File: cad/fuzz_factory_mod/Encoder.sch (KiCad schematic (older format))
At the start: 15 parts

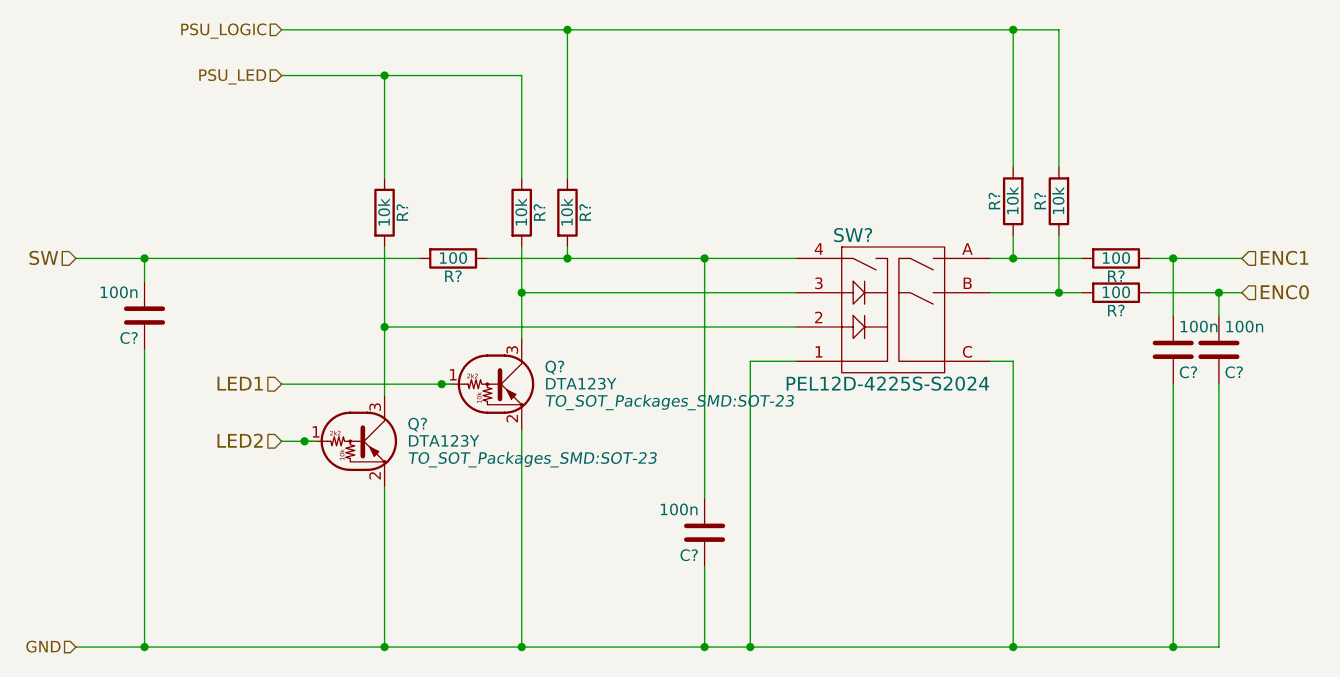
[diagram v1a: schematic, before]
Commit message: Continued schematic.
Modified fuuz_factory circuit : use of matched transistor pairs.
Added USB interface, through FT230X and direct to MCU.
Associated footprints, except for XTAL and trimmers.
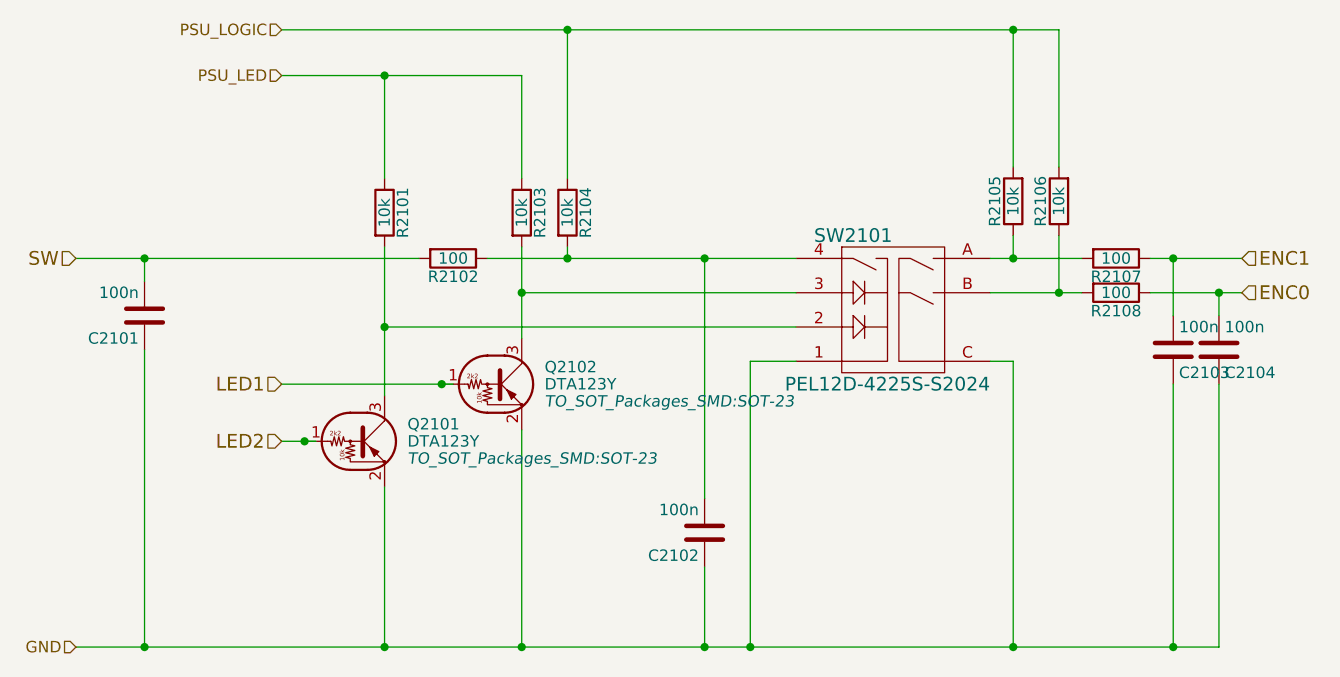
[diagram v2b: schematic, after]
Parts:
- C1901, C1902, C1903, C1904: renamed from C?; footprint Capacitors_SMD:C_0805_HandSoldering -> Capacitors_SMD:C_0603
- R1901, R1902, R1903, R1904, R1905, R1906, R1907, R1908: renamed from R?; footprint Resistors_SMD:R_0603_HandSoldering -> Resistors_SMD:R_0603
- gave numbers to parts that had none: 3

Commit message: Continued schematic.
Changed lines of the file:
@@
 $Descr A4 11693 8268
 encoding utf-8
-Sheet 20 22
+Sheet 6 26
 Title ""
 Date ""
@@
 AR Path="/5E083283/5E2DCD79/5E256B56" Ref="SW2001"  Part="1"
 AR Path="/5E083283/5E2E8544/5E256B56" Ref="SW2101"  Part="1"
-F 0 "SW2101" H 5900 4300 60  0000 C CNN
+AR Path="/5DE4AD26/5EEFDD5E/5E243285/5E256B56" Ref="SW601"  Part="1"
+AR Path="/5DE4AD26/5EEFDD5E/5E2DCD79/5E256B56" Ref="SW701"  Part="1"
+AR Path="/5DE4AD26/5EEFDD5E/5E2E8544/5E256B56" Ref="SW801"  Part="1"
+F 0 "SW801" H 5900 4300 60  0000 C CNN
 F 1 "PEL12D-4225S-S2024" H 6050 3650 60  0000 C CNN
 F 2 "flax_lib:PEL12D" H 5900 4300 60  0001 C CNN
@@
 AR Path="/5E083283/5E2DCD79/5E256B67" Ref="Q2002"  Part="1"
 AR Path="/5E083283/5E2E8544/5E256B67" Ref="Q2102"  Part="1"
-F 0 "Q2102" H 4550 3925 50  0000 L CNN
+AR Path="/5DE4AD26/5EEFDD5E/5E243285/5E256B67" Ref="Q606"  Part="1"
+AR Path="/5DE4AD26/5EEFDD5E/5E2DCD79/5E256B67" Ref="Q702"  Part="1"
+AR Path="/5DE4AD26/5EEFDD5E/5E2E8544/5E256B67" Ref="Q804"  Part="1"
+F 0 "Q804" H 4550 3925 50  0000 L CNN
 F 1 "DTA123Y" H 4550 3850 50  0000 L CNN
 F 2 "TO_SOT_Packages_SMD:SOT-23" H 4550 3775 50  0000 L CIN
@@
 AR Path="/5E083283/5E2DCD79/5E256B6D" Ref="Q2001"  Part="1"
 AR Path="/5E083283/5E2E8544/5E256B6D" Ref="Q2101"  Part="1"
-F 0 "Q2101" H 3950 4175 50  0000 L CNN
+AR Path="/5DE4AD26/5EEFDD5E/5E243285/5E256B6D" Ref="Q605"  Part="1"
+AR Path="/5DE4AD26/5EEFDD5E/5E2DCD79/5E256B6D" Ref="Q701"  Part="1"
+AR Path="/5DE4AD26/5EEFDD5E/5E2E8544/5E256B6D" Ref="Q803"  Part="1"
+F 0 "Q803" H 3950 4175 50  0000 L CNN
 F 1 "DTA123Y" H 3950 4100 50  0000 L CNN
 F 2 "TO_SOT_Packages_SMD:SOT-23" H 3950 4025 50  0000 L CIN
@@
 AR Path="/5E083283/5E2DCD79/5E256B73" Ref="R2004"  Part="1"
 AR Path="/5E083283/5E2E8544/5E256B73" Ref="R2104"  Part="1"
-F 0 "R2104" V 4730 3100 50  0000 C CNN
+AR Path="/5DE4AD26/5EEFDD5E/5E243285/5E256B73" Ref="R620"  Part="1"
+AR Path="/5DE4AD26/5EEFDD5E/5E2DCD79/5E256B73" Ref="R704"  Part="1"
+AR Path="/5DE4AD26/5EEFDD5E/5E2E8544/5E256B73" Ref="R817"  Part="1"
+F 0 "R817" V 4730 3100 50  0000 C CNN
 F 1 "10k" V 4650 3100 50  0000 C CNN
 F 2 "Resistors_SMD:R_0603" V 4580 3100 50  0001 C CNN
@@
 AR Path="/5E083283/5E2DCD79/5E256B79" Ref="R2003"  Part="1"
 AR Path="/5E083283/5E2E8544/5E256B79" Ref="R2103"  Part="1"
-F 0 "R2103" V 4530 3100 50  0000 C CNN
+AR Path="/5DE4AD26/5EEFDD5E/5E243285/5E256B79" Ref="R619"  Part="1"
+AR Path="/5DE4AD26/5EEFDD5E/5E2DCD79/5E256B79" Ref="R703"  Part="1"
+AR Path="/5DE4AD26/5EEFDD5E/5E2E8544/5E256B79" Ref="R816"  Part="1"
+F 0 "R816" V 4530 3100 50  0000 C CNN
 F 1 "10k" V 4450 3100 50  0000 C CNN
 F 2 "Resistors_SMD:R_0603" V 4380 3100 50  0001 C CNN
@@
 AR Path="/5E083283/5E2DCD79/5E256B7F" Ref="R2001"  Part="1"
 AR Path="/5E083283/5E2E8544/5E256B7F" Ref="R2101"  Part="1"
-F 0 "R2101" V 3930 3100 50  0000 C CNN
+AR Path="/5DE4AD26/5EEFDD5E/5E243285/5E256B7F" Ref="R617"  Part="1"
+AR Path="/5DE4AD26/5EEFDD5E/5E2DCD79/5E256B7F" Ref="R701"  Part="1"
+AR Path="/5DE4AD26/5EEFDD5E/5E2E8544/5E256B7F" Ref="R814"  Part="1"
+F 0 "R814" V 3930 3100 50  0000 C CNN
 F 1 "10k" V 3850 3100 50  0000 C CNN
 F 2 "Resistors_SMD:R_0603" V 3780 3100 50  0001 C CNN
@@
 AR Path="/5E083283/5E2DCD79/5E256BA3" Ref="C2002"  Part="1"
 AR Path="/5E083283/5E2E8544/5E256BA3" Ref="C2102"  Part="1"
-F 0 "C2102" H 5275 4600 50  0000 L CNN
+AR Path="/5DE4AD26/5EEFDD5E/5E243285/5E256BA3" Ref="C611"  Part="1"
+AR Path="/5DE4AD26/5EEFDD5E/5E2DCD79/5E256BA3" Ref="C704"  Part="1"
+AR Path="/5DE4AD26/5EEFDD5E/5E2E8544/5E256BA3" Ref="C805"  Part="1"
+F 0 "C805" H 5275 4600 50  0000 L CNN
 F 1 "100n" H 5275 4400 50  0000 L CNN
 F 2 "Capacitors_SMD:C_0603" H 5288 4350 50  0001 C CNN
@@
 AR Path="/5E083283/5E2DCD79/5E256BAF" Ref="R2007"  Part="1"
 AR Path="/5E083283/5E2E8544/5E256BAF" Ref="R2107"  Part="1"
-F 0 "R2107" V 7130 3300 50  0000 C CNN
+AR Path="/5DE4AD26/5EEFDD5E/5E243285/5E256BAF" Ref="R623"  Part="1"
+AR Path="/5DE4AD26/5EEFDD5E/5E2DCD79/5E256BAF" Ref="R707"  Part="1"
+AR Path="/5DE4AD26/5EEFDD5E/5E2E8544/5E256BAF" Ref="R820"  Part="1"
+F 0 "R820" V 7130 3300 50  0000 C CNN
 F 1 "100" V 7050 3300 50  0000 C CNN
 F 2 "Resistors_SMD:R_0603" V 6980 3300 50  0001 C CNN
@@
 AR Path="/5E083283/5E2DCD79/5E256BB5" Ref="R2008"  Part="1"
 AR Path="/5E083283/5E2E8544/5E256BB5" Ref="R2108"  Part="1"
-F 0 "R2108" V 7130 3450 50  0000 C CNN
+AR Path="/5DE4AD26/5EEFDD5E/5E243285/5E256BB5" Ref="R624"  Part="1"
+AR Path="/5DE4AD26/5EEFDD5E/5E2DCD79/5E256BB5" Ref="R708"  Part="1"
+AR Path="/5DE4AD26/5EEFDD5E/5E2E8544/5E256BB5" Ref="R821"  Part="1"
+F 0 "R821" V 7130 3450 50  0000 C CNN
 F 1 "100" V 7050 3450 50  0000 C CNN
 F 2 "Resistors_SMD:R_0603" V 6980 3450 50  0001 C CNN
@@
 AR Path="/5E083283/5E2DCD79/5E256BBB" Ref="C2003"  Part="1"
 AR Path="/5E083283/5E2E8544/5E256BBB" Ref="C2103"  Part="1"
-F 0 "C2103" H 7325 3800 50  0000 L CNN
+AR Path="/5DE4AD26/5EEFDD5E/5E243285/5E256BBB" Ref="C612"  Part="1"
+AR Path="/5DE4AD26/5EEFDD5E/5E2DCD79/5E256BBB" Ref="C705"  Part="1"
+AR Path="/5DE4AD26/5EEFDD5E/5E2E8544/5E256BBB" Ref="C806"  Part="1"
+F 0 "C806" H 7325 3800 50  0000 L CNN
 F 1 "100n" H 7325 3600 50  0000 L CNN
 F 2 "Capacitors_SMD:C_0603" H 7338 3550 50  0001 C CNN
@@
 AR Path="/5E083283/5E2DCD79/5E256BC1" Ref="C2004"  Part="1"
 AR Path="/5E083283/5E2E8544/5E256BC1" Ref="C2104"  Part="1"
-F 0 "C2104" H 7525 3800 50  0000 L CNN
+AR Path="/5DE4AD26/5EEFDD5E/5E243285/5E256BC1" Ref="C613"  Part="1"
+AR Path="/5DE4AD26/5EEFDD5E/5E2DCD79/5E256BC1" Ref="C706"  Part="1"
+AR Path="/5DE4AD26/5EEFDD5E/5E2E8544/5E256BC1" Ref="C807"  Part="1"
+F 0 "C807" H 7525 3800 50  0000 L CNN
 F 1 "100n" H 7525 3600 50  0000 L CNN
 F 2 "Capacitors_SMD:C_0603" H 7538 3550 50  0001 C CNN
@@
 AR Path="/5E083283/5E2DCD79/5E256BD9" Ref="R2005"  Part="1"
 AR Path="/5E083283/5E2E8544/5E256BD9" Ref="R2105"  Part="1"
-F 0 "R2105" V 6680 3050 50  0000 C CNN
+AR Path="/5DE4AD26/5EEFDD5E/5E243285/5E256BD9" Ref="R621"  Part="1"
+AR Path="/5DE4AD26/5EEFDD5E/5E2DCD79/5E256BD9" Ref="R705"  Part="1"
+AR Path="/5DE4AD26/5EEFDD5E/5E2E8544/5E256BD9" Ref="R818"  Part="1"
+F 0 "R818" V 6680 3050 50  0000 C CNN
 F 1 "10k" V 6600 3050 50  0000 C CNN
 F 2 "Resistors_SMD:R_0603" V 6530 3050 50  0001 C CNN
@@
 AR Path="/5E083283/5E2DCD79/5E256BDF" Ref="R2006"  Part="1"
 AR Path="/5E083283/5E2E8544/5E256BDF" Ref="R2106"  Part="1"
-F 0 "R2106" V 6880 3050 50  0000 C CNN
+AR Path="/5DE4AD26/5EEFDD5E/5E243285/5E256BDF" Ref="R622"  Part="1"
+AR Path="/5DE4AD26/5EEFDD5E/5E2DCD79/5E256BDF" Ref="R706"  Part="1"
+AR Path="/5DE4AD26/5EEFDD5E/5E2E8544/5E256BDF" Ref="R819"  Part="1"
+F 0 "R819" V 6880 3050 50  0000 C CNN
 F 1 "10k" V 6800 3050 50  0000 C CNN
 F 2 "Resistors_SMD:R_0603" V 6730 3050 50  0001 C CNN
@@
 AR Path="/5E083283/5E2DCD79/5E256BF1" Ref="R2002"  Part="1"
 AR Path="/5E083283/5E2E8544/5E256BF1" Ref="R2102"  Part="1"
-F 0 "R2102" V 4230 3300 50  0000 C CNN
+AR Path="/5DE4AD26/5EEFDD5E/5E243285/5E256BF1" Ref="R618"  Part="1"
+AR Path="/5DE4AD26/5EEFDD5E/5E2DCD79/5E256BF1" Ref="R702"  Part="1"
+AR Path="/5DE4AD26/5EEFDD5E/5E2E8544/5E256BF1" Ref="R815"  Part="1"
+F 0 "R815" V 4230 3300 50  0000 C CNN
 F 1 "100" V 4150 3300 50  0000 C CNN
 F 2 "Resistors_SMD:R_0603" V 4080 3300 50  0001 C CNN
@@
 AR Path="/5E083283/5E2DCD79/5E256BF7" Ref="C2001"  Part="1"
 AR Path="/5E083283/5E2E8544/5E256BF7" Ref="C2101"  Part="1"
-F 0 "C2101" H 2825 3650 50  0000 L CNN
+AR Path="/5DE4AD26/5EEFDD5E/5E243285/5E256BF7" Ref="C610"  Part="1"
+AR Path="/5DE4AD26/5EEFDD5E/5E2DCD79/5E256BF7" Ref="C703"  Part="1"
+AR Path="/5DE4AD26/5EEFDD5E/5E2E8544/5E256BF7" Ref="C804"  Part="1"
+F 0 "C804" H 2825 3650 50  0000 L CNN
 F 1 "100n" H 2825 3450 50  0000 L CNN
 F 2 "Capacitors_SMD:C_0603" H 2838 3400 50  0001 C CNN
